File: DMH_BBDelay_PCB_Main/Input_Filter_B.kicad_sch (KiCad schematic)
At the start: 14 parts, among them U21 TL072

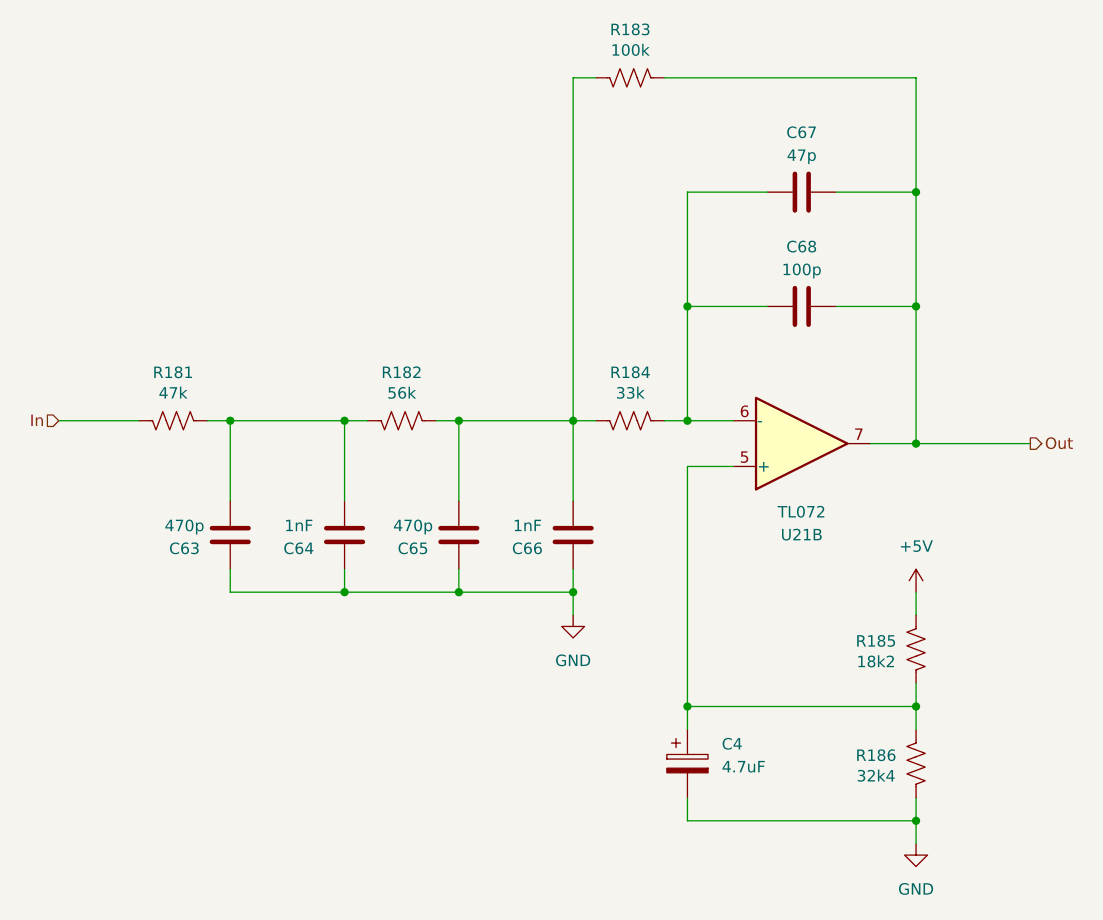
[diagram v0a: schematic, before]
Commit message: Added output filter to channel B
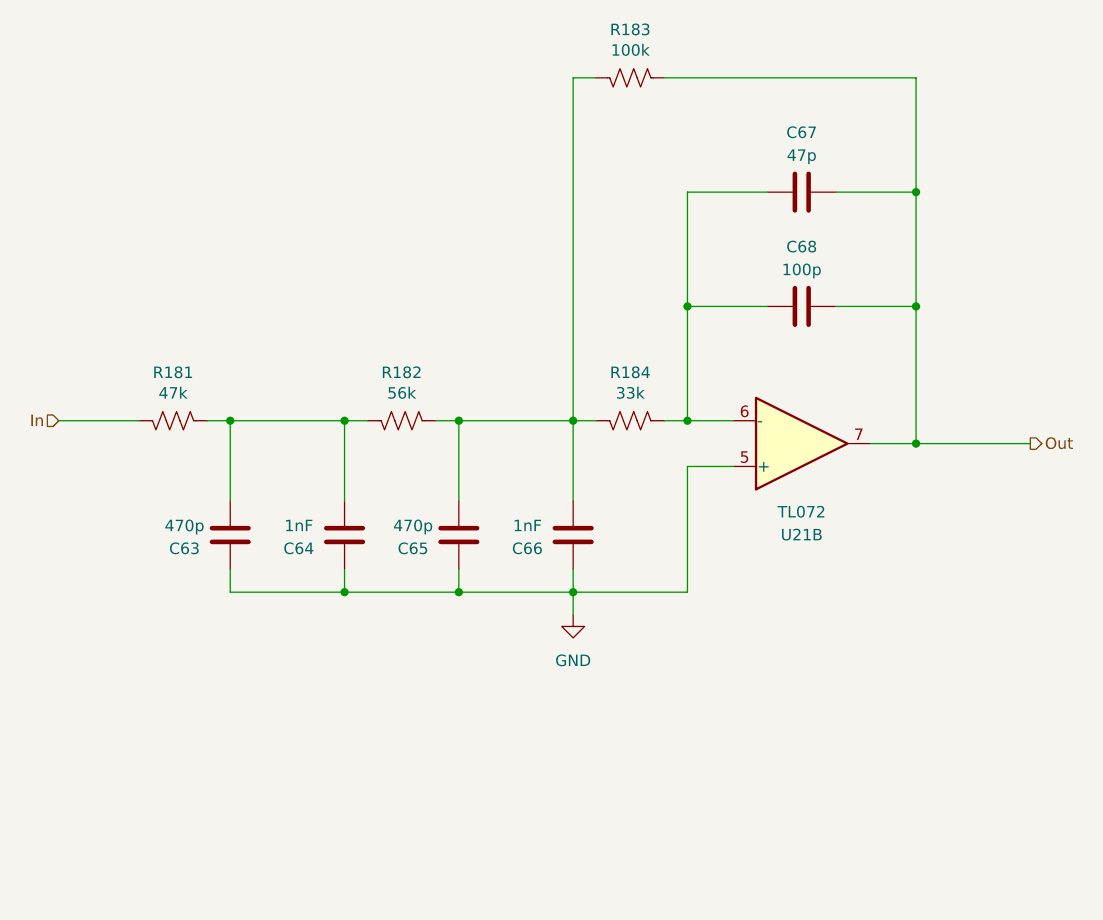
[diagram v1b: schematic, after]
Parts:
- removed C4: 4.7uF, Capacitor_THT:CP_Radial_D5.0mm_P2.00mm, symbol Device:C_Polarized
- removed R185: 18k2, Resistor_THT:R_Axial_DIN0207_L6.3mm_D2.5mm_P7.62mm_Horizontal, symbol Device:R_US
- removed R186: 32k4, Resistor_THT:R_Axial_DIN0207_L6.3mm_D2.5mm_P7.62mm_Horizontal, symbol Device:R_US
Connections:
- net GND: now also U21.5 (+)
